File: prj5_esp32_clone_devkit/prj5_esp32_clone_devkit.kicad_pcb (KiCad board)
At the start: 4 copper layers, 0 parts

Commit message: Posizionati i footprint
Feat: creato un primo posizionamento finale per i componenti
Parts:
- added C1: 22uF/10V(20%), Capacitor_SMD:C_0603_1608Metric, B.Cu at (160.0, 107.1)
- added C14: 0.1uF/50V(10%), Capacitor_SMD:C_0402_1005Metric, F.Cu at (162.2, 110.7)
- added C15: 0.1uF/50V(10%)(NC), Capacitor_SMD:C_0402_1005Metric, F.Cu at (142.2, 110.7)
- added C19: 0.1uf/50V(10%), Capacitor_SMD:C_0402_1005Metric, F.Cu at (148.5, 107.4)
- added C20: 4.7uf/6.3V(10%), Capacitor_SMD:C_0402_1005Metric, F.Cu at (146.7, 103.9)
- added C21: 22uF/10V(20%), Capacitor_SMD:C_0603_1608Metric, F.Cu at (144.2, 107.4)
- added C22: 0.1uF/50V(10%), Capacitor_SMD:C_0402_1005Metric, F.Cu at (143.3, 103.9)
- added C3: 22uF/10V(20%), Capacitor_SMD:C_0603_1608Metric, B.Cu at (160.0, 103.8)
- added C9: 0.1uF/50V(10%), Capacitor_SMD:C_0402_1005Metric, F.Cu at (150.2, 103.9)
- added D1: LED, LED_SMD:LED_0603_1608Metric, F.Cu at (152.1, 100.3)
- added D3: D_Schottky, Diode_SMD:D_SOD-323, F.Cu at (160.9, 100.3)
- added D4: D_TVS, Diode_SMD:D_SOD-523, F.Cu at (156.4, 100.3)
- added D5: D_TVS, Diode_SMD:D_SOD-523, F.Cu at (147.7, 100.3)
- added D6: D_TVS, Diode_SMD:D_SOD-523, F.Cu at (143.6, 100.3)
- added J1: USB_B_Micro, Connector_USB:USB_Micro-AB_Molex_47590-0001, F.Cu at (152.4, 125.0)
- added J2: Conn_01x19_Pin, Connector_PinHeader_2.54mm:PinHeader_1x19_P2.54mm_Vertical, F.Cu at (138.9, 79.9)
- added J3: Conn_01x19_Pin, Connector_PinHeader_2.54mm:PinHeader_1x19_P2.54mm_Vertical, F.Cu at (165.9, 79.9)
- added MOD1: ESP32-WROOM-32, digikey-footprints:ESP32-WROOM-32D, F.Cu at (152.4, 86.7)
- added Q1: MMSS8050-H-TP, digikey-footprints:SOT-23-3, F.Cu at (143.9, 123.1)
- added Q2: MMSS8050-H-TP, digikey-footprints:SOT-23-3, F.Cu at (160.8, 123.1)
- added R11: 10K(5%), Resistor_SMD:R_01005_0402Metric, F.Cu at (152.0, 107.4)
- added R17: 0R(5%), Resistor_SMD:R_01005_0402Metric, F.Cu at (156.1, 103.9)
- added R18: 0R(5%), Resistor_SMD:R_01005_0402Metric, F.Cu at (158.3, 107.4)
- added R2: 2K(5%), Resistor_SMD:R_01005_0402Metric, F.Cu at (155.2, 107.4)
- added R21: 10K(5%), Resistor_SMD:R_01005_0402Metric, F.Cu at (160.8, 126.9)
- added R22: 10K(5%), Resistor_SMD:R_01005_0402Metric, F.Cu at (144.0, 126.9)
- added R23: 10K(5%)(NC), Resistor_SMD:R_01005_0402Metric, F.Cu at (159.0, 103.9)
- added R24: 2K(5%), Resistor_SMD:R_01005_0402Metric, F.Cu at (153.3, 103.9)
- added R25: 22.1K(5%), Resistor_SMD:R_01005_0402Metric, F.Cu at (161.8, 103.9)
- added R28: 47.5K(5%), Resistor_SMD:R_01005_0402Metric, F.Cu at (161.5, 107.4)
- added SW1: SW_Push, Button_Switch_SMD:SW_SPST_B3S-1000, F.Cu at (146.2, 116.1)
- added SW2: SW_Push, Button_Switch_SMD:SW_SPST_B3S-1000, F.Cu at (158.6, 116.1)
- added U1: CP2102N-A01-GQFN28, Package_DFN_QFN:TQFN-28-1EP_5x5mm_P0.5mm_EP2.7x2.7mm, B.Cu at (152.4, 115.4)
- added U2: AMS1117-3.3, Package_TO_SOT_SMD:SOT-223-3_TabPin2, B.Cu at (152.4, 104.1)
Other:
- board outline added: 31.2 x 57.4 mm

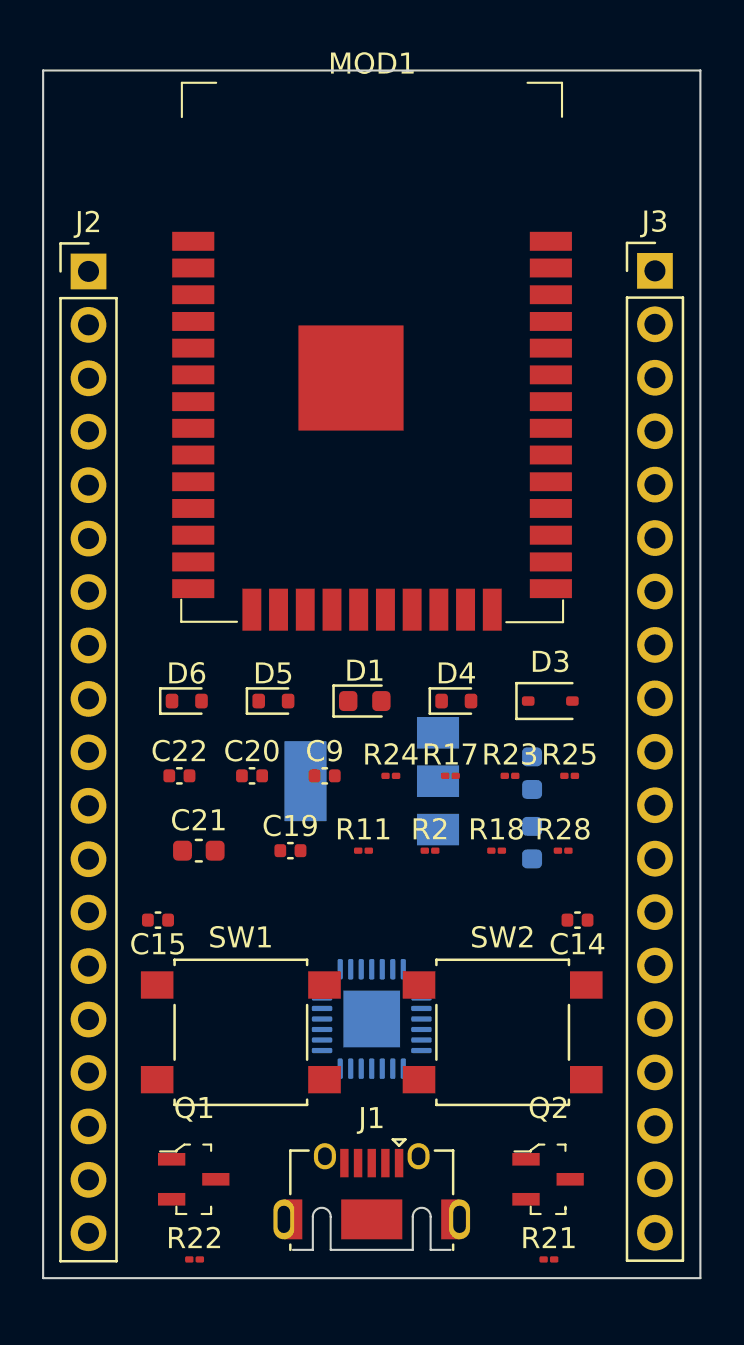
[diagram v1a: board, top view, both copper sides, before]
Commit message: Correzione errori clearance e simboli
Fix: corretto F.Courtyard di MOD1
Fix: corretto Edge.Cuts di J1
Fix: modificato board setup per avere conformi i componenti 0402
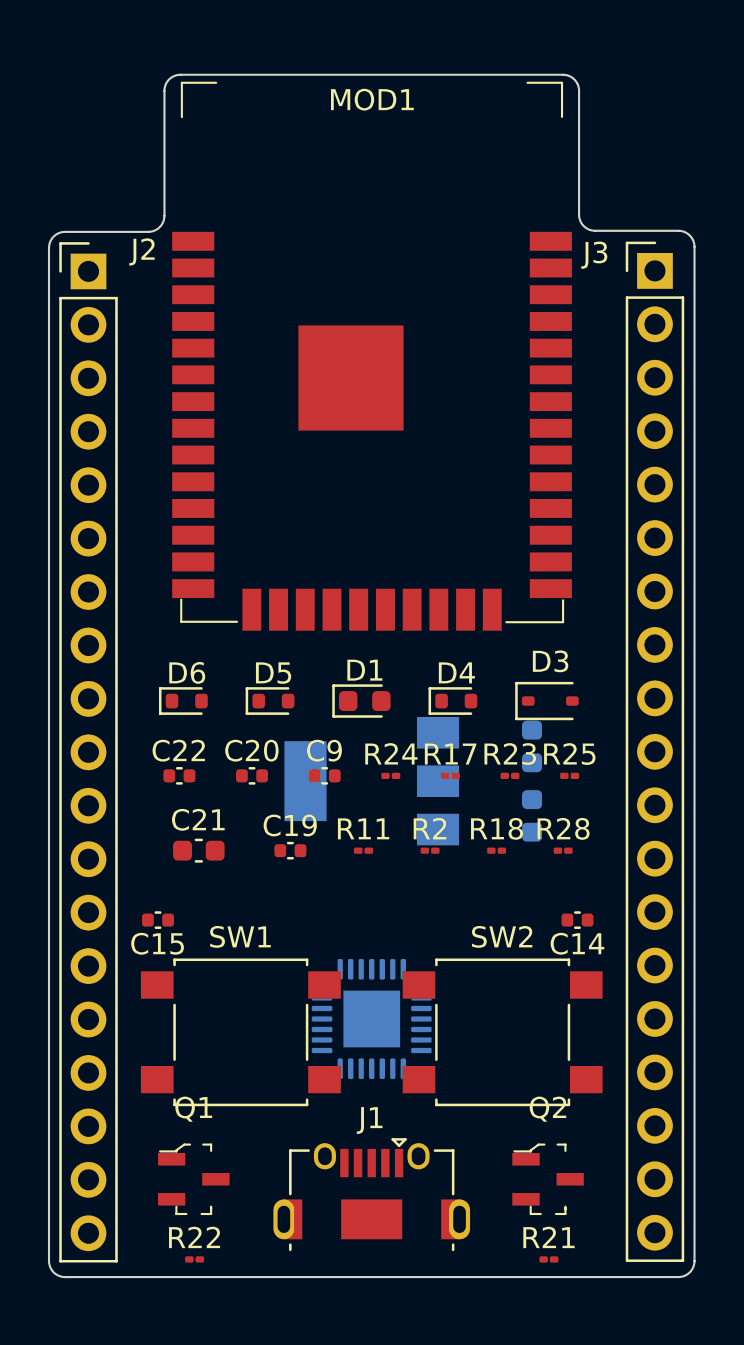
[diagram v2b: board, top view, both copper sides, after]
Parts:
- moved C1 1.27 mm to (160.0, 105.8)
- moved C3 1.27 mm to (160.0, 102.5)
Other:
- board size 31.2 x 57.4 mm -> 30.7 x 57.2 mm
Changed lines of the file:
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@@
     (fp_line (start 3.87 1.2) (end 3.87 1.45)
       (stroke (width 0.12) (type solid)) (layer "F.SilkS"))
-    (fp_line (start -3.75 1.45) (end -2.8 1.45)
-      (stroke (width 0.1) (type solid)) (layer "Edge.Cuts"))
-    (fp_line (start -2.8 -0.125) (end -2.8 1.45)
-      (stroke (width 0.1) (type solid)) (layer "Edge.Cuts"))
-    (fp_line (start -1.95 -0.125) (end -1.95 1.45)
-      (stroke (width 0.1) (type solid)) (layer "Edge.Cuts"))
-    (fp_line (start -1.95 1.45) (end 1.95 1.45)
-      (stroke (width 0.1) (type solid)) (layer "Edge.Cuts"))
-    (fp_line (start 1.95 -0.125) (end 1.95 1.45)
-      (stroke (width 0.1) (type solid)) (layer "Edge.Cuts"))
-    (fp_line (start 2.8 -0.125) (end 2.8 1.45)
-      (stroke (width 0.1) (type solid)) (layer "Edge.Cuts"))
-    (fp_line (start 2.8 1.45) (end 3.75 1.45)
-      (stroke (width 0.1) (type solid)) (layer "Edge.Cuts"))
-    (fp_arc (start -2.8 -0.125) (mid -2.375 -0.55) (end -1.95 -0.125)
-      (stroke (width 0.1) (type solid)) (layer "Edge.Cuts"))
-    (fp_arc (start 1.95 -0.125) (mid 2.375 -0.55) (end 2.8 -0.125)
-      (stroke (width 0.1) (type solid)) (layer "Edge.Cuts"))
     (fp_line (start -5.18 -4.13) (end -5.18 2.65)
       (stroke (width 0.05) (type solid)) (layer "F.CrtYd"))
@@
     (property "ki_keywords" "connector")
     (attr through_hole)
-    (fp_text reference "J2" (at 0 -2.33) (layer "F.SilkS")
+    (fp_text reference "J2" (at 2.6434 -1.016) (layer "F.SilkS")
         (effects (font (size 1 1) (thickness 0.15)))
     )
@@
     (property "ki_keywords" "connector")
     (attr through_hole)
-    (fp_text reference "J3" (at 0 -2.33) (layer "F.SilkS")
+    (fp_text reference "J3" (at -2.794 -0.8382) (layer "F.SilkS")
         (effects (font (size 1 1) (thickness 0.15)))
     )
@@
     (property "ki_keywords" "1904-1010-1-ND *")
     (attr smd)
-    (fp_text reference "MOD1" (at 0.01 -16.69) (layer "F.SilkS")
+    (fp_text reference "MOD1" (at 0.01 -14.9516) (layer "F.SilkS")
         (effects (font (size 1 1) (thickness 0.15)))
     )
@@
     (fp_line (start 9.08 9.85) (end 6.38 9.85)
       (stroke (width 0.1) (type solid)) (layer "F.SilkS"))
-    (fp_line (start -9.77 -16.04) (end -9.77 10.47)
-      (stroke (width 0.1) (type solid)) (layer "F.CrtYd"))
-    (fp_line (start -9.77 10.47) (end 9.73 10.46)
-      (stroke (width 0.1) (type solid)) (layer "F.CrtYd"))
-    (fp_line (start 9.74 -16.04) (end -9.74 -16.04)
-      (stroke (width 0.1) (type solid)) (layer "F.CrtYd"))
-    (fp_line (start 9.74 10.46) (end 9.74 -16.02)
-      (stroke (width 0.1) (type solid)) (layer "F.CrtYd"))
+    (fp_rect (start -9.652 -16.002) (end 9.652 10.414)
+      (stroke (width 0.05) (type default)) (fill none) (layer "F.CrtYd"))
     (fp_line (start -9 -15.748) (end -9 9.755)
       (stroke (width 0.1) (type solid)) (layer "F.Fab"))
@@
   )
   (footprint "Capacitor_SMD:C_0603_1608Metric" (layer "B.Cu")
-    (at 160.02 103.759 90)
+    (at 160.02 102.489 90)
     (descr "Capacitor SMD 0603 (1608 Metric), square (rectangular) end terminal, IPC_7351 nominal, (Body size source: IPC-SM-782 page 76, https://www.pcb-3d.com/wordpress/wp-content/uploads/ipc-sm-782a_amendment_1_and_2.pdf), generated with kicad-footprint-generator")
     (tags "capacitor")
@@
   )
   (footprint "Capacitor_SMD:C_0603_1608Metric" (layer "B.Cu")
-    (at 160.02 107.061 90)
+    (at 160.02 105.791 90)
     (descr "Capacitor SMD 0603 (1608 Metric), square (rectangular) end terminal, IPC_7351 nominal, (Body size source: IPC-SM-782 page 76, https://www.pcb-3d.com/wordpress/wp-content/uploads/ipc-sm-782a_amendment_1_and_2.pdf), generated with kicad-footprint-generator")
     (tags "capacitor")
@@
     )
   )
-  (gr_rect (start 136.779 70.358) (end 168.021 127.762)
-    (stroke (width 0.1) (type default)) (fill none) (layer "Edge.Cuts"))
+  (gr_arc (start 137.0584 78.7908) (mid 137.281585 78.251985) (end 137.8204 78.0288)
+    (stroke (width 0.1) (type default)) (layer "Edge.Cuts"))
+  (gr_line (start 167.7416 126.9492) (end 167.7416 78.74)
+    (stroke (width 0.1) (type default)) (layer "Edge.Cuts"))
+  (gr_line (start 166.9796 77.978) (end 163.0172 77.978)
+    (stroke (width 0.1) (type default)) (layer "Edge.Cuts"))
+  (gr_arc (start 142.5448 71.3232) (mid 142.767985 70.784385) (end 143.3068 70.5612)
+    (stroke (width 0.1) (type default)) (layer "Edge.Cuts"))
+  (gr_line (start 161.4932 70.5612) (end 143.3068 70.5612)
+    (stroke (width 0.1) (type default)) (layer "Edge.Cuts"))
+  (gr_arc (start 167.7416 126.9492) (mid 167.518415 127.488015) (end 166.9796 127.7112)
+    (stroke (width 0.1) (type default)) (layer "Edge.Cuts"))
+  (gr_arc (start 142.5448 77.2668) (mid 142.321615 77.805615) (end 141.7828 78.0288)
+    (stroke (width 0.1) (type default)) (layer "Edge.Cuts"))
+  (gr_line (start 142.5448 71.3232) (end 142.5448 77.2668)
+    (stroke (width 0.1) (type default)) (layer "Edge.Cuts"))
+  (gr_line (start 141.7828 78.0288) (end 137.8204 78.0288)
+    (stroke (width 0.1) (type default)) (layer "Edge.Cuts"))
+  (gr_line (start 162.2552 77.216) (end 162.2552 71.3232)
+    (stroke (width 0.1) (type default)) (layer "Edge.Cuts"))
+  (gr_arc (start 163.0172 77.978) (mid 162.478385 77.754815) (end 162.2552 77.216)
+    (stroke (width 0.1) (type default)) (layer "Edge.Cuts"))
+  (gr_arc (start 166.9796 77.978) (mid 167.518415 78.201185) (end 167.7416 78.74)
+    (stroke (width 0.1) (type default)) (layer "Edge.Cuts"))
+  (gr_line (start 137.0584 78.7908) (end 137.0584 126.9492)
+    (stroke (width 0.1) (type default)) (layer "Edge.Cuts"))
+  (gr_arc (start 137.8204 127.7112) (mid 137.281585 127.488015) (end 137.0584 126.9492)
+    (stroke (width 0.1) (type default)) (layer "Edge.Cuts"))
+  (gr_line (start 137.8204 127.7112) (end 166.9796 127.7112)
+    (stroke (width 0.1) (type default)) (layer "Edge.Cuts"))
+  (gr_arc (start 161.4932 70.5612) (mid 162.032015 70.784385) (end 162.2552 71.3232)
+    (stroke (width 0.1) (type default)) (layer "Edge.Cuts"))
 )

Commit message: Connessioni footprint e fix
Feat: create gran parte delle connessioni su Pcbnew
Fix: sistemato il track width della classe POWER
Fix: sistemata connessione nello schematico, mancava label DTR su pin 28 di U1
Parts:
- moved R22 16.8 mm to (160.8, 126.9)
- moved R21 16.8 mm to (144.0, 126.9), turned to 180 degrees
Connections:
- U1 pad 28: unconnected-(U1-DTR-Pad28) -> /DTR
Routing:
- net GND: track 0.00 -> 148.2 mm, vias 0 -> 1
- net /VDD33: track 0.00 -> 87.0 mm, vias 0 -> 5
- net /EN: track 0.00 -> 79.6 mm, vias 0 -> 7
- net /IO0: track 0.00 -> 73.1 mm, vias 0 -> 1
- net /EXT_5V: track 0.00 -> 56.4 mm, vias 0 -> 2
- net /VBUS: track 0.00 -> 56.0 mm, vias 0 -> 4
- net /DTR: track 0.00 -> 40.8 mm, vias 0 -> 2
- net /RTS: track 0.00 -> 39.9 mm, vias 0 -> 1
- net /CMD: track 0.00 -> 37.0 mm
- net /SD0: track 0.00 -> 35.9 mm
- net /CLK: track 0.00 -> 35.3 mm, vias 0 -> 1
- net /USB_DP: track 0.00 -> 34.3 mm, vias 0 -> 3
- net /SD3: track 0.00 -> 33.4 mm
- net /SD1: track 0.00 -> 32.3 mm
- net /RXD0: track 0.00 -> 31.4 mm, vias 0 -> 1
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
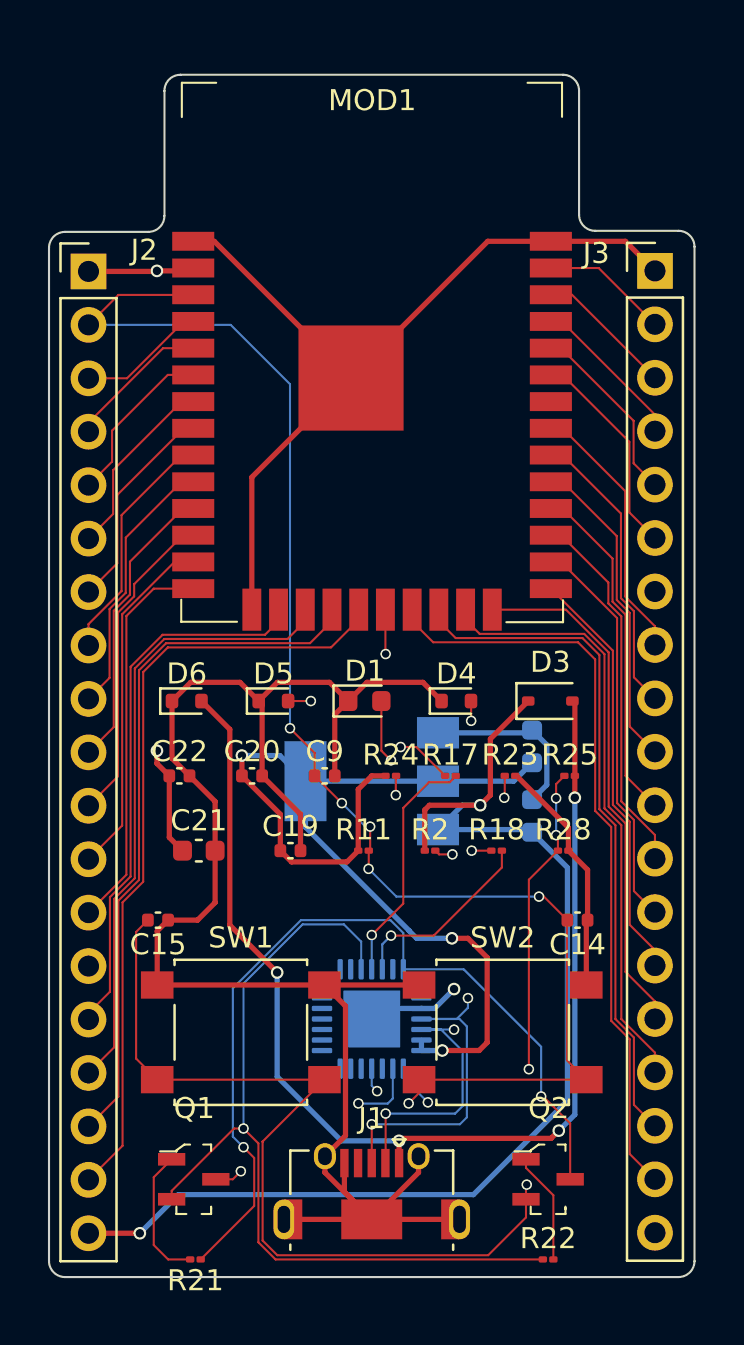
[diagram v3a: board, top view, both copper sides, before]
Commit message: Rimossi tutti gli errori di connessioni
Feat: creato copper fill per GND
Feat: creato copper fill per VDD33
Feat: creata keepout zone sotto all'antenna
Fix: corrette connessioni mancanti
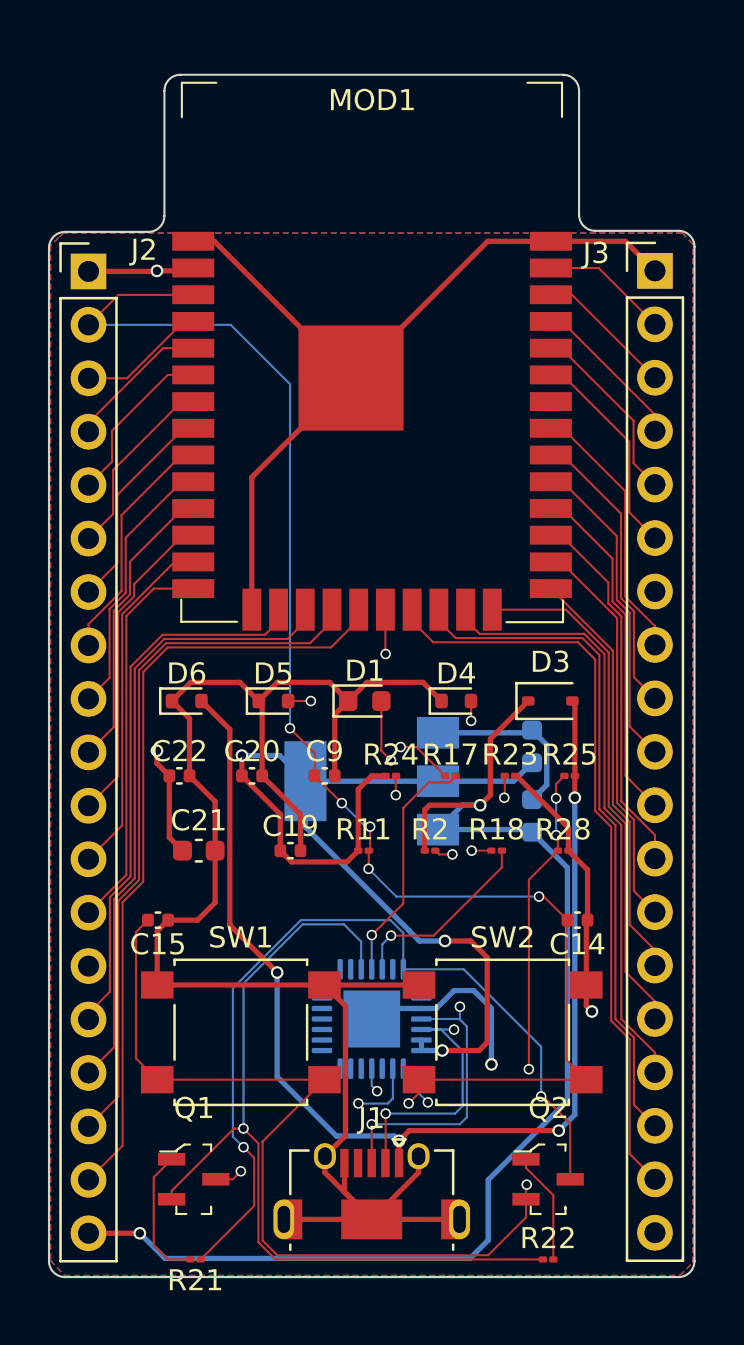
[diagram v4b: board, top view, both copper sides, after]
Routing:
- net GND: track 148.2 -> 154.4 mm, vias 1 -> 2
- net /EXT_5V: track 56.4 -> 59.1 mm
- net /USB_DP: track 34.3 -> 32.3 mm
- added copper zone on F.Cu, net /VDD33
- added copper zone on B.Cu, net GND

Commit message: Completamento aggiustamenti silkscreen e connessioni
Feat: aggiunti loghi in silkscreen
Fix: sistemati i posizionamenti delle silkscreen
Fix: corretta silkscreen di Q1 e Q2 (footprint)
Fix: corretta la traccia GND di U1
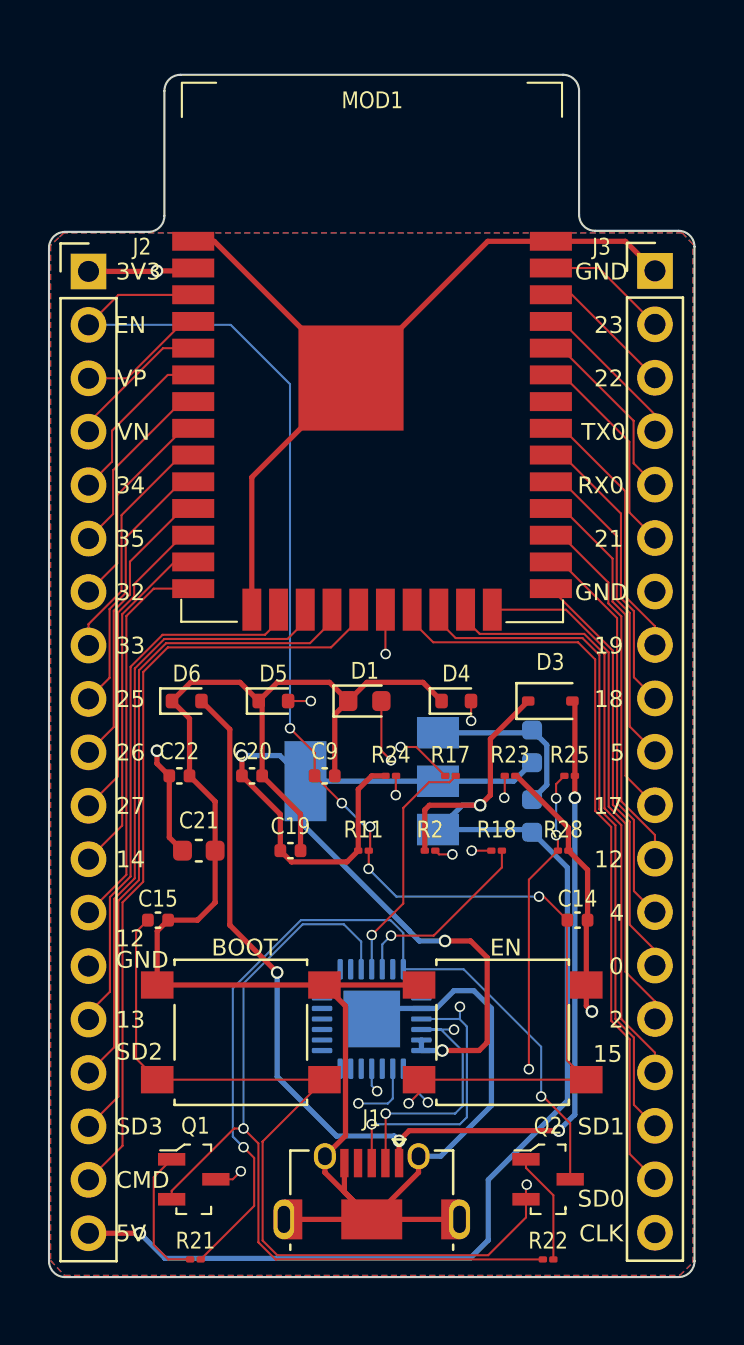
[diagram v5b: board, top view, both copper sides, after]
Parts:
- added G1: LOGO, The_Electronic_Music_Project_silk_logo:The_Electronic_Music_Project_silk_logo, B.Cu at (157.8, 74.4)
- added REF1: KiCad-Logo2_5mm_SilkScreen, Symbol:KiCad-Logo2_5mm_SilkScreen, B.Cu at (152.4, 91.8)
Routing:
- net GND: track 154.4 -> 160.8 mm, vias 2 -> 1
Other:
- board text added: "0"
- board text added: "12"
- board text added: "13"
- board text added: "14"
- board text added: "15"
- board text added: "17"
- board text added: "18"
- board text added: "19"
- board text added: "2"
- board text added: "21"
- board text added: "22"
- board text added: "23"
- board text added: "25"
- board text added: "26"
- board text added: "27"
- board text added: "32"
- board text added: "33"
- board text added: "34"
- board text added: "35"
- board text added: "3V3"
- board text added: "4"
- board text added: "5"
- board text added: "5V"
- board text added: "BOOT"
- board text added: "CLK"
- board text added: "CMD"
- board text added: "EN"
- board text added: "ESP32 Devkit v4 Custom PCB"
- board text added: "GND"
- board text added: "RX0"
- board text added: "SD0"
- board text added: "SD1"
- board text added: "SD2"
- board text added: "SD3"
- board text added: "TX0"
- board text added: "VN"
- board text added: "VP"
